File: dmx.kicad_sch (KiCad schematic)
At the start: 37 parts, among them J102 CORTEX-DEBUG, J103 JAE_DX07S016JA3, SW101 SW_Push, SW102 SW_Push, U101 TPS78433QWDRBRQ1, U102 ATSAMD51G, Y101 32k768

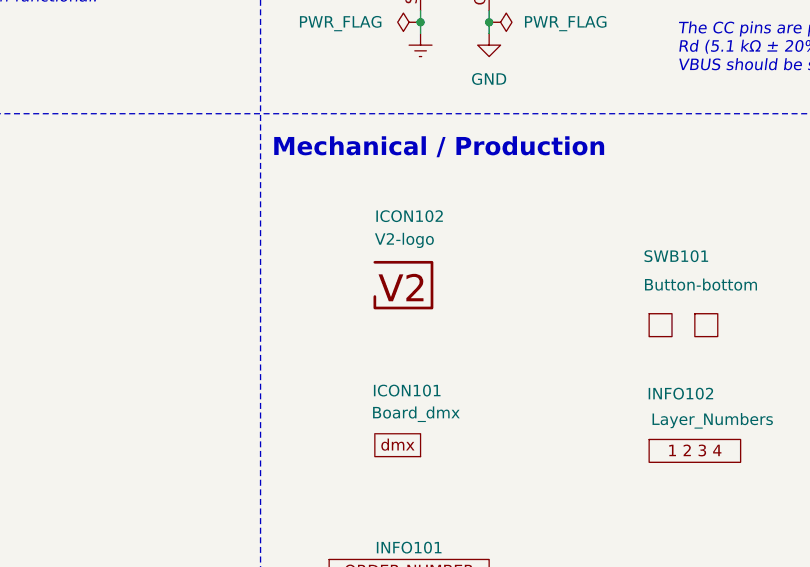
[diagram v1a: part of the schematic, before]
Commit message: Update TRS socket
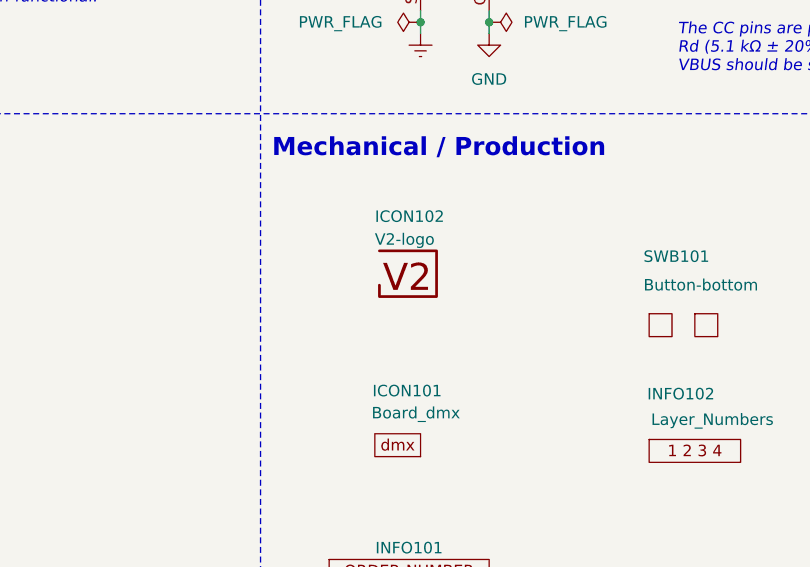
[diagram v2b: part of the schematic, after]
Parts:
- U101: value TPS78433QWDRBRQ1 -> TPS78433QWDRBRQ1
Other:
- moved on the sheet: ICON102
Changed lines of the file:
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@@
 	(title_block
 		(title "V2 dmx")
-		(date "2023-01-07")
-		(rev "2")
+		(date "2024-07-17")
+		(rev "3")
 		(company "Versio Duo")
 		(comment 1 "MIDI to DMX Bridge")
@@
 			)
 		)
-		(property "Value" "TPS78433QWDRBRQ1 "
+		(property "Value" "TPS78433QWDRBRQ1"
 			(at 193.04 29.21 0)
 			(effects
